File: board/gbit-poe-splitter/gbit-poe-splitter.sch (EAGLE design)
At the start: 50 parts, among them IC1 LM2596HVS, U1 TPS2379DDA

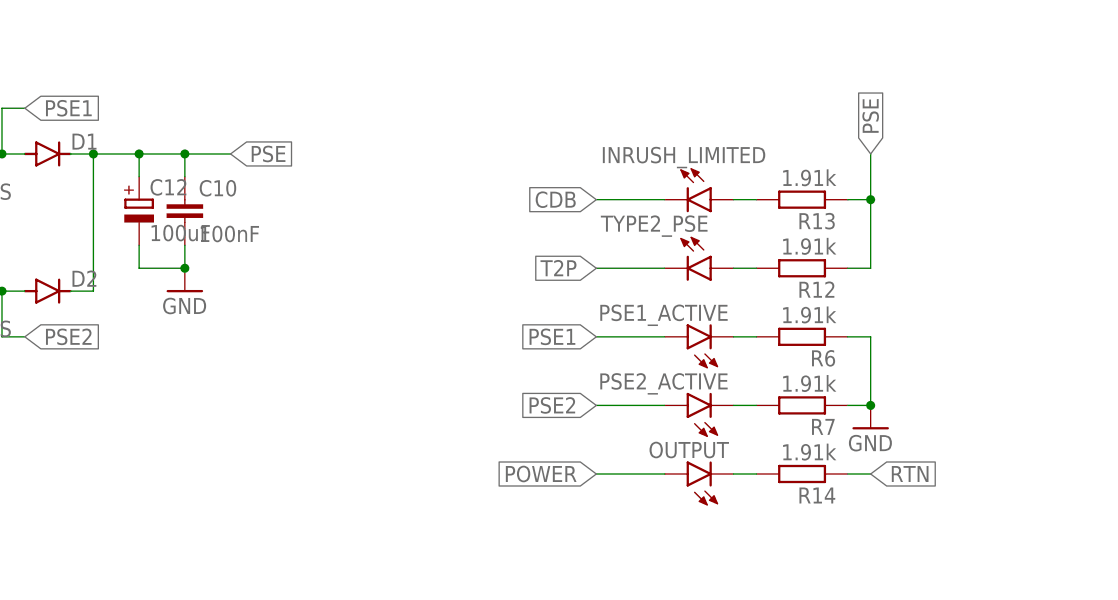
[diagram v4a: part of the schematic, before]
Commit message: Wrote first prototype summary and added partial fixes to layout
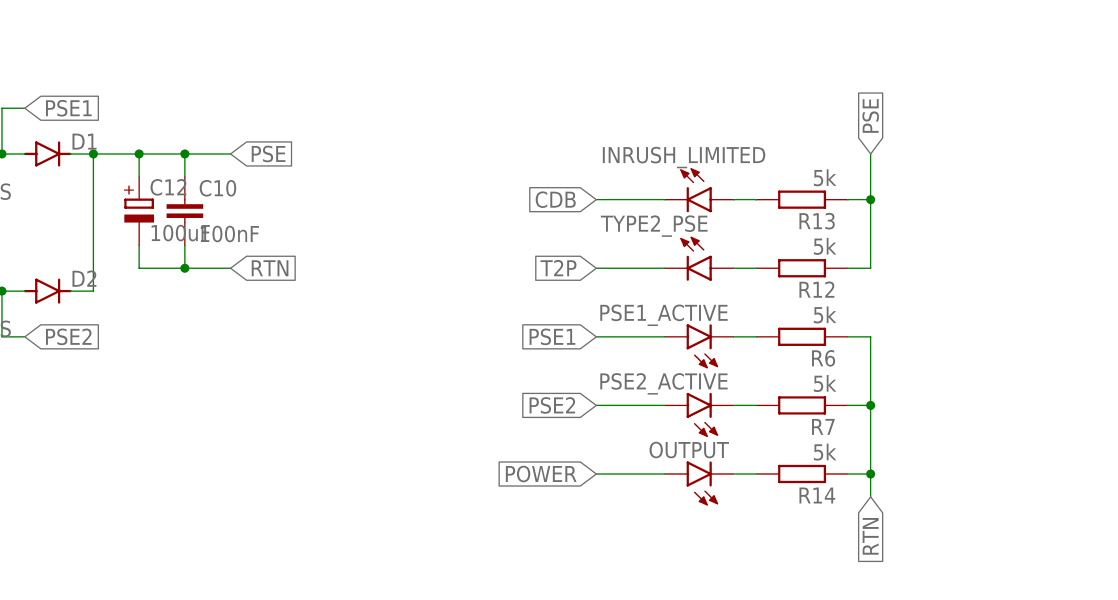
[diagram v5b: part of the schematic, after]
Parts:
- R12, R13, R14, R6, R7: value 1.91k -> 5k
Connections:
- net GND: no longer C10.2, C12.-, R6.1, R7.1
- net RTN: now also C10.2, C12.-, R6.1, R7.1
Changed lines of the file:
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@@
 <part name="D1" library="diode" library_urn="urn:adsk.eagle:library:210" deviceset="DIODE-" device="DO-214AC" package3d_urn="urn:adsk.eagle:package:43416/2"/>
 <part name="D2" library="diode" library_urn="urn:adsk.eagle:library:210" deviceset="DIODE-" device="DO-214AC" package3d_urn="urn:adsk.eagle:package:43416/2"/>
-<part name="R6" library="rcl" library_urn="urn:adsk.eagle:library:334" deviceset="R-EU_" device="R0603" package3d_urn="urn:adsk.eagle:package:23555/3" value="1.91k"/>
-<part name="R7" library="rcl" library_urn="urn:adsk.eagle:library:334" deviceset="R-EU_" device="R0603" package3d_urn="urn:adsk.eagle:package:23555/3" value="1.91k"/>
-<part name="GND5" library="supply1" library_urn="urn:adsk.eagle:library:371" deviceset="GND" device=""/>
-<part name="R12" library="rcl" library_urn="urn:adsk.eagle:library:334" deviceset="R-EU_" device="R0603" package3d_urn="urn:adsk.eagle:package:23555/3" value="1.91k"/>
-<part name="R13" library="rcl" library_urn="urn:adsk.eagle:library:334" deviceset="R-EU_" device="R0603" package3d_urn="urn:adsk.eagle:package:23555/3" value="1.91k"/>
+<part name="R6" library="rcl" library_urn="urn:adsk.eagle:library:334" deviceset="R-EU_" device="R0603" package3d_urn="urn:adsk.eagle:package:23555/3" value="5k"/>
+<part name="R7" library="rcl" library_urn="urn:adsk.eagle:library:334" deviceset="R-EU_" device="R0603" package3d_urn="urn:adsk.eagle:package:23555/3" value="5k"/>
+<part name="R12" library="rcl" library_urn="urn:adsk.eagle:library:334" deviceset="R-EU_" device="R0603" package3d_urn="urn:adsk.eagle:package:23555/3" value="5k"/>
+<part name="R13" library="rcl" library_urn="urn:adsk.eagle:library:334" deviceset="R-EU_" device="R0603" package3d_urn="urn:adsk.eagle:package:23555/3" value="5k"/>
 <part name="INRUSH_LIMITED" library="led" library_urn="urn:adsk.eagle:library:259" deviceset="LED" device="CHIPLED_0603" package3d_urn="urn:adsk.eagle:package:15822/2"/>
-<part name="R14" library="rcl" library_urn="urn:adsk.eagle:library:334" deviceset="R-EU_" device="R0603" package3d_urn="urn:adsk.eagle:package:23555/3" value="1.91k"/>
+<part name="R14" library="rcl" library_urn="urn:adsk.eagle:library:334" deviceset="R-EU_" device="R0603" package3d_urn="urn:adsk.eagle:package:23555/3" value="5k"/>
 <part name="C10" library="rcl" library_urn="urn:adsk.eagle:library:334" deviceset="C-EU" device="C0805" package3d_urn="urn:adsk.eagle:package:23617/2" value="100nF"/>
-<part name="GND6" library="supply1" library_urn="urn:adsk.eagle:library:371" deviceset="GND" device=""/>
 <part name="R1" library="rcl" library_urn="urn:adsk.eagle:library:334" deviceset="R-EU_" device="R0603" package3d_urn="urn:adsk.eagle:package:23555/3" value="1.27k"/>
 <part name="R15" library="rcl" library_urn="urn:adsk.eagle:library:334" deviceset="R-EU_" device="R0603" package3d_urn="urn:adsk.eagle:package:23555/3" value="243R"/>
@@
 <attribute name="VALUE" x="87.63" y="8.382" size="1.778" layer="96" rot="R180"/>
 </instance>
-<instance part="GND5" gate="1" x="91.44" y="2.54" smashed="yes" grouprefs="STATUS_LEDS">
-<attribute name="VALUE" x="88.9" y="0" size="1.778" layer="96"/>
-</instance>
 <instance part="R12" gate="G$1" x="83.82" y="20.32" smashed="yes" rot="R180" grouprefs="STATUS_LEDS">
 <attribute name="NAME" x="87.63" y="18.8214" size="1.778" layer="95" rot="R180"/>
@@
 <attribute name="NAME" x="16.764" y="28.321" size="1.778" layer="95"/>
 <attribute name="VALUE" x="16.764" y="23.241" size="1.778" layer="96"/>
-</instance>
-<instance part="GND6" gate="1" x="15.24" y="17.78" smashed="yes" grouprefs="POWER_ROUTER">
-<attribute name="VALUE" x="12.7" y="15.24" size="1.778" layer="96"/>
 </instance>
 <instance part="R1" gate="G$1" x="10.16" y="81.28" smashed="yes" rot="R180" grouprefs="POE_CLS_JUMPERS">
@@
 <junction x="-22.86" y="17.78" grouprefs="POWER_ROUTER"/>
 <pinref part="GND4" gate="1" pin="GND"/>
-</segment>
-<segment>
-<pinref part="R6" gate="G$1" pin="1"/>
-<wire x1="88.9" y1="12.7" x2="91.44" y2="12.7" width="0.1524" layer="91" grouprefs="STATUS_LEDS"/>
-<wire x1="91.44" y1="12.7" x2="91.44" y2="5.08" width="0.1524" layer="91" grouprefs="STATUS_LEDS"/>
-<pinref part="R7" gate="G$1" pin="1"/>
-<wire x1="91.44" y1="5.08" x2="88.9" y2="5.08" width="0.1524" layer="91" grouprefs="STATUS_LEDS"/>
-<junction x="91.44" y="5.08" grouprefs="STATUS_LEDS"/>
-<pinref part="GND5" gate="1" pin="GND"/>
-</segment>
-<segment>
-<pinref part="C10" gate="G$1" pin="2"/>
-<wire x1="15.24" y1="22.86" x2="15.24" y2="20.32" width="0.1524" layer="91" grouprefs="POWER_ROUTER"/>
-<pinref part="GND6" gate="1" pin="GND"/>
-<pinref part="C12" gate="G$1" pin="-"/>
-<wire x1="10.16" y1="22.86" x2="10.16" y2="20.32" width="0.1524" layer="91" grouprefs="POWER_ROUTER"/>
-<wire x1="10.16" y1="20.32" x2="15.24" y2="20.32" width="0.1524" layer="91" grouprefs="POWER_ROUTER"/>
-<junction x="15.24" y="20.32" grouprefs="POWER_ROUTER"/>
 </segment>
 <segment>
@@
 <pinref part="R14" gate="G$1" pin="1"/>
 <wire x1="88.9" y1="-2.54" x2="91.44" y2="-2.54" width="0.1524" layer="91"/>
-<label x="91.44" y="-2.54" size="1.778" layer="95" xref="yes"/>
-</segment>
-</net>
+<pinref part="R6" gate="G$1" pin="1"/>
+<wire x1="88.9" y1="12.7" x2="91.44" y2="12.7" width="0.1524" layer="91" grouprefs="STATUS_LEDS"/>
+<wire x1="91.44" y1="12.7" x2="91.44" y2="5.08" width="0.1524" layer="91" grouprefs="STATUS_LEDS"/>
+<pinref part="R7" gate="G$1" pin="1"/>
+<wire x1="91.44" y1="5.08" x2="88.9" y2="5.08" width="0.1524" layer="91" grouprefs="STATUS_LEDS"/>
+<wire x1="91.44" y1="5.08" x2="91.44" y2="-2.54" width="0.1524" layer="91"/>
+<junction x="91.44" y="5.08"/>
+<wire x1="91.44" y1="-2.54" x2="91.44" y2="-5.08" width="0.1524" layer="91"/>
+<junction x="91.44" y="-2.54"/>
+<label x="91.44" y="-5.08" size="1.778" layer="95" rot="R270" xref="yes" grouprefs="STATUS_LEDS"/>
+</segment>
+<segment>
+<pinref part="C10" gate="G$1" pin="2"/>
+<wire x1="15.24" y1="22.86" x2="15.24" y2="20.32" width="0.1524" layer="91" grouprefs="POWER_ROUTER"/>
+<pinref part="C12" gate="G$1" pin="-"/>
+<wire x1="10.16" y1="22.86" x2="10.16" y2="20.32" width="0.1524" layer="91" grouprefs="POWER_ROUTER"/>
+<wire x1="10.16" y1="20.32" x2="15.24" y2="20.32" width="0.1524" layer="91" grouprefs="POWER_ROUTER"/>
+<wire x1="15.24" y1="20.32" x2="20.32" y2="20.32" width="0.1524" layer="91"/>
+<junction x="15.24" y="20.32"/>
+<label x="20.32" y="20.32" size="1.778" layer="95" xref="yes"/>
+</segment>
+</net>

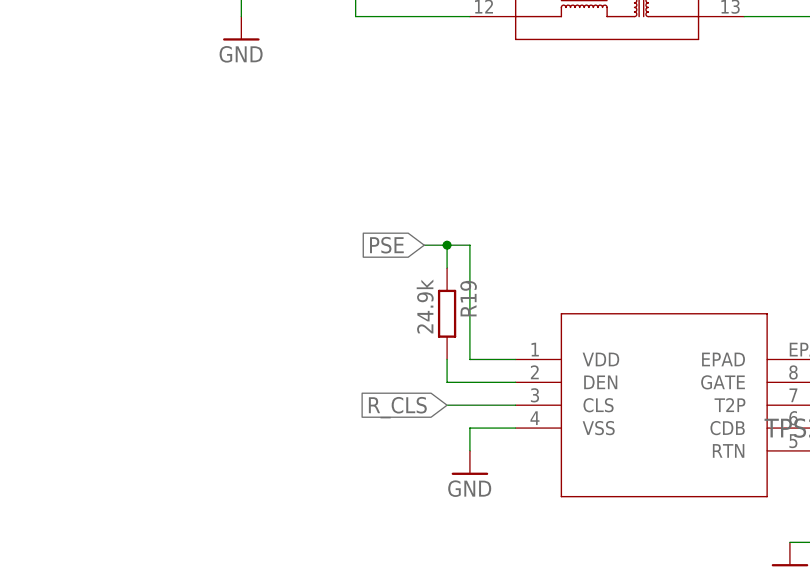
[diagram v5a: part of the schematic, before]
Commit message: Fixed layout issues
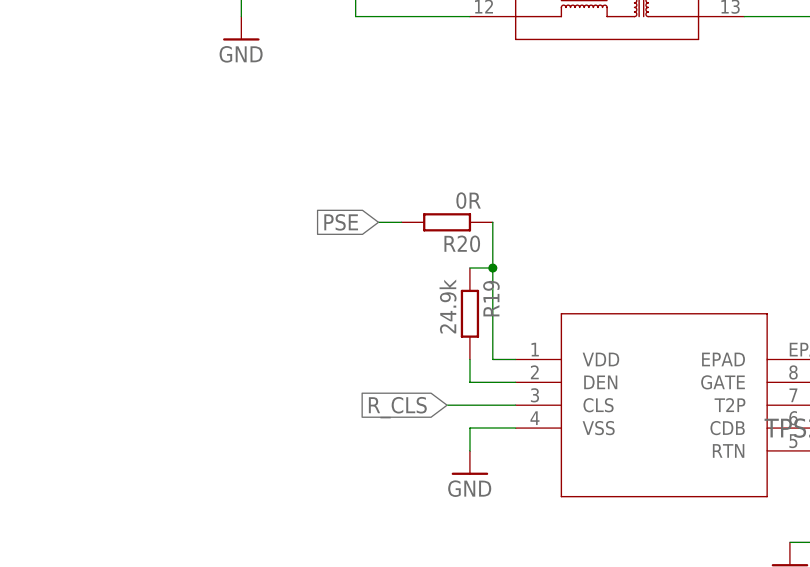
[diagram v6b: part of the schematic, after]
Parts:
- added R20: 0R, rcl:R-EU_R1206
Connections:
- new net N$38: R19.1, R20.1, U1.VDD
- net PSE: now also R20.2; no longer R19.1, U1.VDD
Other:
- moved on the sheet: R19
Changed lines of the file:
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@@
 <part name="U$3" library="TRIM_CA6_VSMD" deviceset="TRIM_CA6_VSMD" device=""/>
 <part name="J3" library="con-jack" library_urn="urn:adsk.eagle:library:154" deviceset="DCJ0303" device="" package3d_urn="urn:adsk.eagle:package:7493/1"/>
+<part name="R20" library="rcl" library_urn="urn:adsk.eagle:library:334" deviceset="R-EU_" device="R1206" package3d_urn="urn:adsk.eagle:package:23540/2" value="0R"/>
 </parts>
 <sheets>
@@
 <attribute name="VALUE" x="15.24" y="60.96" size="1.778" layer="96"/>
 </instance>
-<instance part="R19" gate="G$1" x="-116.84" y="33.02" smashed="yes" rot="R270" grouprefs="POE_CONTROLLER">
-<attribute name="NAME" x="-115.3414" y="36.83" size="1.778" layer="95" rot="R270"/>
-<attribute name="VALUE" x="-120.142" y="36.83" size="1.778" layer="96" rot="R270"/>
+<instance part="R19" gate="G$1" x="-114.3" y="33.02" smashed="yes" rot="R270" grouprefs="POE_CONTROLLER">
+<attribute name="NAME" x="-112.8014" y="36.83" size="1.778" layer="95" rot="R270"/>
+<attribute name="VALUE" x="-117.602" y="36.83" size="1.778" layer="96" rot="R270"/>
 </instance>
 <instance part="GND8" gate="1" x="-114.3" y="15.24" smashed="yes" grouprefs="POE_CONTROLLER">
@@
 <attribute name="NAME" x="-20.32" y="113.03" size="1.778" layer="95"/>
 <attribute name="VALUE" x="-20.32" y="102.87" size="1.778" layer="96"/>
+</instance>
+<instance part="R20" gate="G$1" x="-116.84" y="43.18" smashed="yes" rot="R180">
+<attribute name="NAME" x="-113.03" y="41.6814" size="1.778" layer="95" rot="R180"/>
+<attribute name="VALUE" x="-113.03" y="46.482" size="1.778" layer="96" rot="R180"/>
 </instance>
 </instances>
@@
 </segment>
 <segment>
-<pinref part="R19" gate="G$1" pin="1"/>
-<wire x1="-116.84" y1="38.1" x2="-116.84" y2="40.64" width="0.1524" layer="91" grouprefs="POE_CONTROLLER"/>
-<wire x1="-116.84" y1="40.64" x2="-114.3" y2="40.64" width="0.1524" layer="91" grouprefs="POE_CONTROLLER"/>
-<pinref part="U1" gate="A" pin="VDD"/>
-<wire x1="-109.22" y1="27.94" x2="-114.3" y2="27.94" width="0.1524" layer="91" grouprefs="POE_CONTROLLER"/>
-<wire x1="-114.3" y1="27.94" x2="-114.3" y2="40.64" width="0.1524" layer="91" grouprefs="POE_CONTROLLER"/>
-<wire x1="-116.84" y1="40.64" x2="-119.38" y2="40.64" width="0.1524" layer="91" grouprefs="POE_CONTROLLER"/>
-<junction x="-116.84" y="40.64" grouprefs="POE_CONTROLLER"/>
-<label x="-119.38" y="40.64" size="1.778" layer="95" rot="R180" xref="yes" grouprefs="POE_CONTROLLER"/>
+<wire x1="-121.92" y1="43.18" x2="-124.46" y2="43.18" width="0.1524" layer="91" grouprefs="POE_CONTROLLER"/>
+<label x="-124.46" y="43.18" size="1.778" layer="95" rot="R180" xref="yes" grouprefs="POE_CONTROLLER"/>
+<pinref part="R20" gate="G$1" pin="2"/>
 </segment>
 <segment>
@@
 <segment>
 <pinref part="R19" gate="G$1" pin="2"/>
-<wire x1="-116.84" y1="27.94" x2="-116.84" y2="25.4" width="0.1524" layer="91" grouprefs="POE_CONTROLLER"/>
+<wire x1="-114.3" y1="27.94" x2="-114.3" y2="25.4" width="0.1524" layer="91" grouprefs="POE_CONTROLLER"/>
 <pinref part="U1" gate="A" pin="DEN"/>
-<wire x1="-116.84" y1="25.4" x2="-109.22" y2="25.4" width="0.1524" layer="91" grouprefs="POE_CONTROLLER"/>
+<wire x1="-114.3" y1="25.4" x2="-109.22" y2="25.4" width="0.1524" layer="91" grouprefs="POE_CONTROLLER"/>
 </segment>
 </net>
@@
 </segment>
 </net>
+<net name="N$38" class="0">
+<segment>
+<pinref part="U1" gate="A" pin="VDD"/>
+<wire x1="-109.22" y1="27.94" x2="-111.76" y2="27.94" width="0.1524" layer="91"/>
+<pinref part="R19" gate="G$1" pin="1"/>
+<wire x1="-111.76" y1="38.1" x2="-114.3" y2="38.1" width="0.1524" layer="91"/>
+<wire x1="-111.76" y1="27.94" x2="-111.76" y2="38.1" width="0.1524" layer="91"/>
+<pinref part="R20" gate="G$1" pin="1"/>
+<wire x1="-111.76" y1="43.18" x2="-111.76" y2="38.1" width="0.1524" layer="91"/>
+<junction x="-111.76" y="38.1"/>
+</segment>
+</net>
